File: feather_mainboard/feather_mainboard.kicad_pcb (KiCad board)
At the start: 2 copper layers, 60 x 60 mm, 42 parts, among them J1 62501021721, J2 62501021721, J3 61300211121, J4 693071020811, J5 61300211121, J6 61300211121, J7 61300211121, J8 61300211121, U1 Adafruit ESP32-S3 Feather, U2 SI2307CDS-T1-BE3, U3 2N7002K-T1-GE3, U4 WPME-FISM_SMT-8

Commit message: Corrected/switched the names of MISO and MOSI pins
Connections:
- net /MicroSD-Card Adapter/SD_MISO/CMD renamed /MicroSD-Card Adapter/SD_MOSI/CMD
- net /MicroSD-Card Adapter/SD_MOSI/DAT0 renamed /MicroSD-Card Adapter/SD_MISO/DAT0
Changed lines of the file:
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@@
 	(net 19 "Net-(J6-Pad1)")
 	(net 20 "Net-(J3-Pad1)")
-	(net 21 "/MicroSD-Card Adapter/SD_MISO{slash}CMD")
+	(net 21 "/MicroSD-Card Adapter/SD_MOSI{slash}CMD")
 	(net 22 "/MicroSD-Card Adapter/SD_DAT2")
 	(net 23 "/MicroSD-Card Adapter/SD_CD")
 	(net 24 "/MicroSD-Card Adapter/SD_CLK")
-	(net 25 "/MicroSD-Card Adapter/SD_MOSI{slash}DAT0")
+	(net 25 "/MicroSD-Card Adapter/SD_MISO{slash}DAT0")
 	(net 26 "/MicroSD-Card Adapter/SD_CS{slash}DAT3")
 	(net 27 "/MicroSD-Card Adapter/SD_DAT1")
@@
 			(size 0.7 1.9)
 			(layers "F.Cu" "F.Paste" "F.Mask")
-			(net 21 "/MicroSD-Card Adapter/SD_MISO{slash}CMD")
+			(net 21 "/MicroSD-Card Adapter/SD_MOSI{slash}CMD")
 			(pinfunction "CMD")
 			(pintype "bidirectional")
@@
 			(size 0.7 1.9)
 			(layers "F.Cu" "F.Paste" "F.Mask")
-			(net 25 "/MicroSD-Card Adapter/SD_MOSI{slash}DAT0")
+			(net 25 "/MicroSD-Card Adapter/SD_MISO{slash}DAT0")
 			(pinfunction "DAT0")
 			(pintype "bidirectional")
@@
 			)
 		)
+		(sheetname "Display-Ports")
+		(sheetfile "display_ports.kicad_sch")
 		(attr through_hole)
 		(fp_line
@@
 			(size 0.6 0.9)
 			(layers "F.Cu" "F.Paste" "F.Mask")
-			(net 21 "/MicroSD-Card Adapter/SD_MISO{slash}CMD")
+			(net 21 "/MicroSD-Card Adapter/SD_MOSI{slash}CMD")
 			(pintype "passive")
 			(solder_mask_margin 0.102)
@@
 			)
 		)
+		(sheetname "Buttons-Connector")
+		(sheetfile "buttons-connector.kicad_sch")
 		(attr through_hole)
 		(fp_line
@@
 			(size 0.6 0.9)
 			(layers "F.Cu" "F.Paste" "F.Mask")
-			(net 25 "/MicroSD-Card Adapter/SD_MOSI{slash}DAT0")
+			(net 25 "/MicroSD-Card Adapter/SD_MISO{slash}DAT0")
 			(pintype "passive")
 			(solder_mask_margin 0.102)
@@
 			(layers "*.Cu" "*.Mask")
 			(remove_unused_layers no)
-			(net 21 "/MicroSD-Card Adapter/SD_MISO{slash}CMD")
+			(net 21 "/MicroSD-Card Adapter/SD_MOSI{slash}CMD")
 			(pinfunction "D13")
 			(pintype "bidirectional")
@@
 			(layers "*.Cu" "*.Mask")
 			(remove_unused_layers no)
-			(net 25 "/MicroSD-Card Adapter/SD_MOSI{slash}DAT0")
+			(net 25 "/MicroSD-Card Adapter/SD_MISO{slash}DAT0")
 			(pinfunction "D11")
 			(pintype "bidirectional")

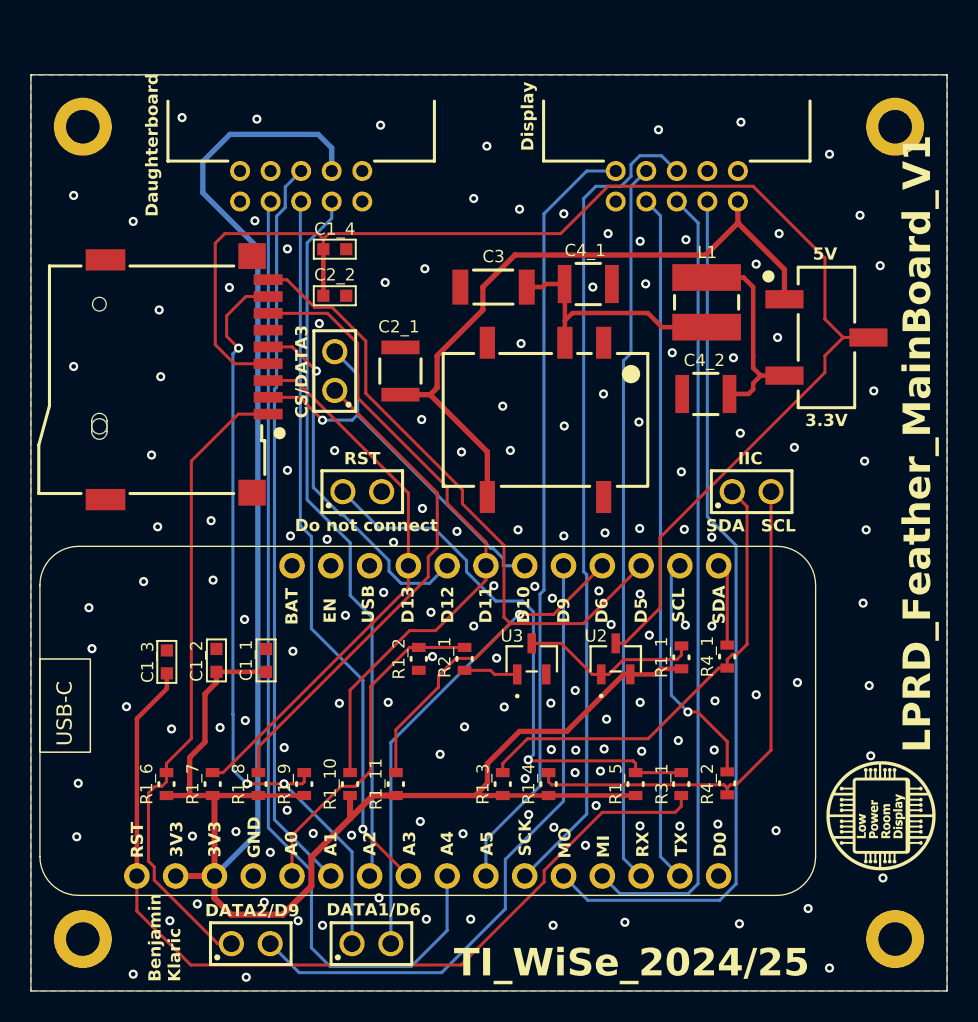
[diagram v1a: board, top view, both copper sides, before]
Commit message: Added V1.1: added a Shottky diode to block the parasitic feedback into the system from the SD adapter; routed the SD adapter pull-ups to the SD Vcc and not the uC Vcc; updated silkscreen text; cleaned routing overall; more vias and more ground plane coverage
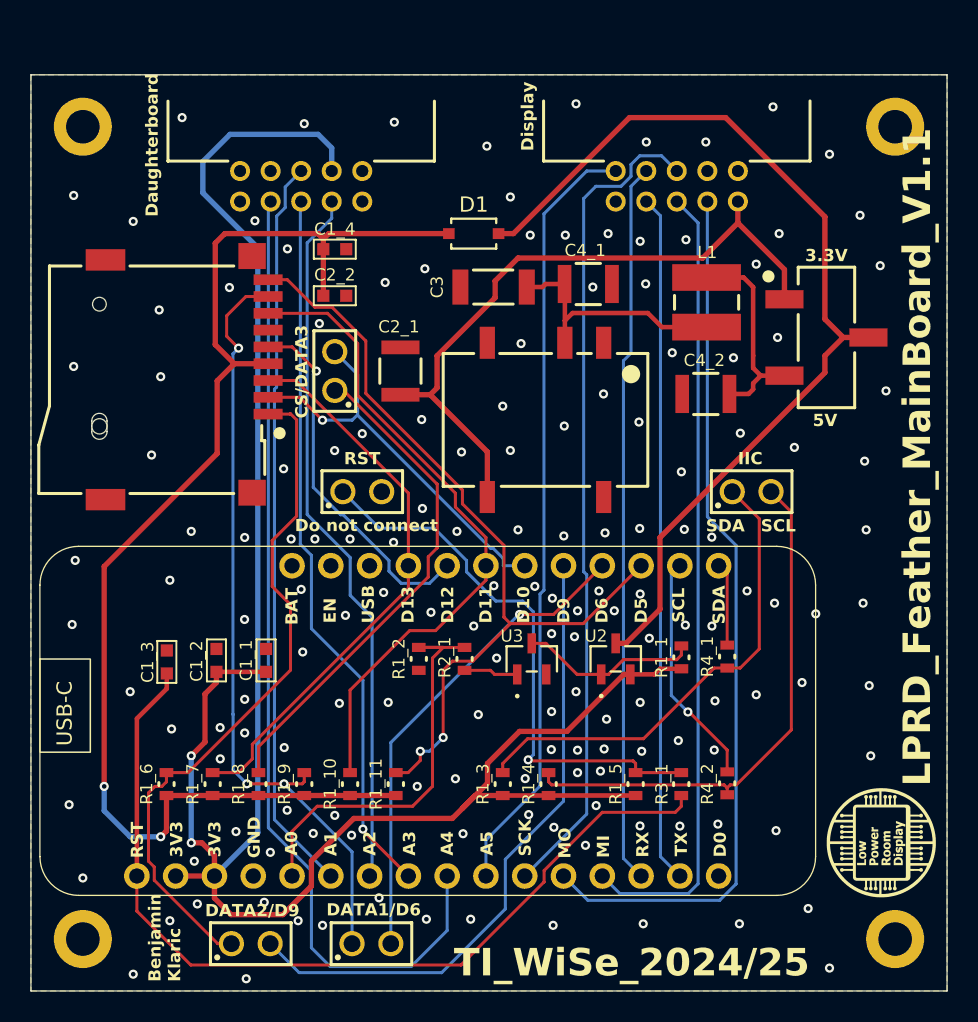
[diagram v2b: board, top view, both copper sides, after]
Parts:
- added D1: PMEG6010CEH_115, Custom footprints:SDO_SOD123F_NEX, F.Cu at (148.8, 79.8)
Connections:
- C1_4 pad 2: /Display-Enable/Switch -> Net-(J4-VDD)
- C2_2 pad 2: /Display-Enable/Switch -> Net-(J4-VDD)
- J4 pad 4: /Display-Enable/Switch -> Net-(J4-VDD)
- R1_10 pad 1: VCC -> Net-(J4-VDD)
- R1_11 pad 1: VCC -> Net-(J4-VDD)
- R1_6 pad 2: VCC -> Net-(J4-VDD)
- R1_7 pad 2: VCC -> Net-(J4-VDD)
- R1_8 pad 2: VCC -> Net-(J4-VDD)
- R1_9 pad 1: VCC -> Net-(J4-VDD)
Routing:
- net Net-(J4-VDD): track 0.00 -> 85.0 mm, vias 0 -> 2
- net /Display-Enable/Switch: track 91.9 -> 63.9 mm
- net VCC: track 142.3 -> 134.0 mm, vias 0 -> 2
- net /Display-Enable/EN: track 22.3 -> 27.3 mm
- net Net-(J4-DAT2): track 42.1 -> 45.2 mm
- net Net-(J6-Pad2): track 33.7 -> 34.8 mm
- net Net-(J6-Pad1): track 30.6 -> 31.5 mm
- net /MicroSD-Card Adapter/SD_CD: track 54.2 -> 55.1 mm, vias 0 -> 2
- net /MicroSD-Card Adapter/SD_MOSI/CMD: track 36.3 -> 36.9 mm
- net GND: vias 147 -> 157
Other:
- board text added: "LPRD_Feather_MainBoard_V1.1"
- board text removed: "LPRD_Feather_MainBoard_V1"

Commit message: Small changes to silkscreen text
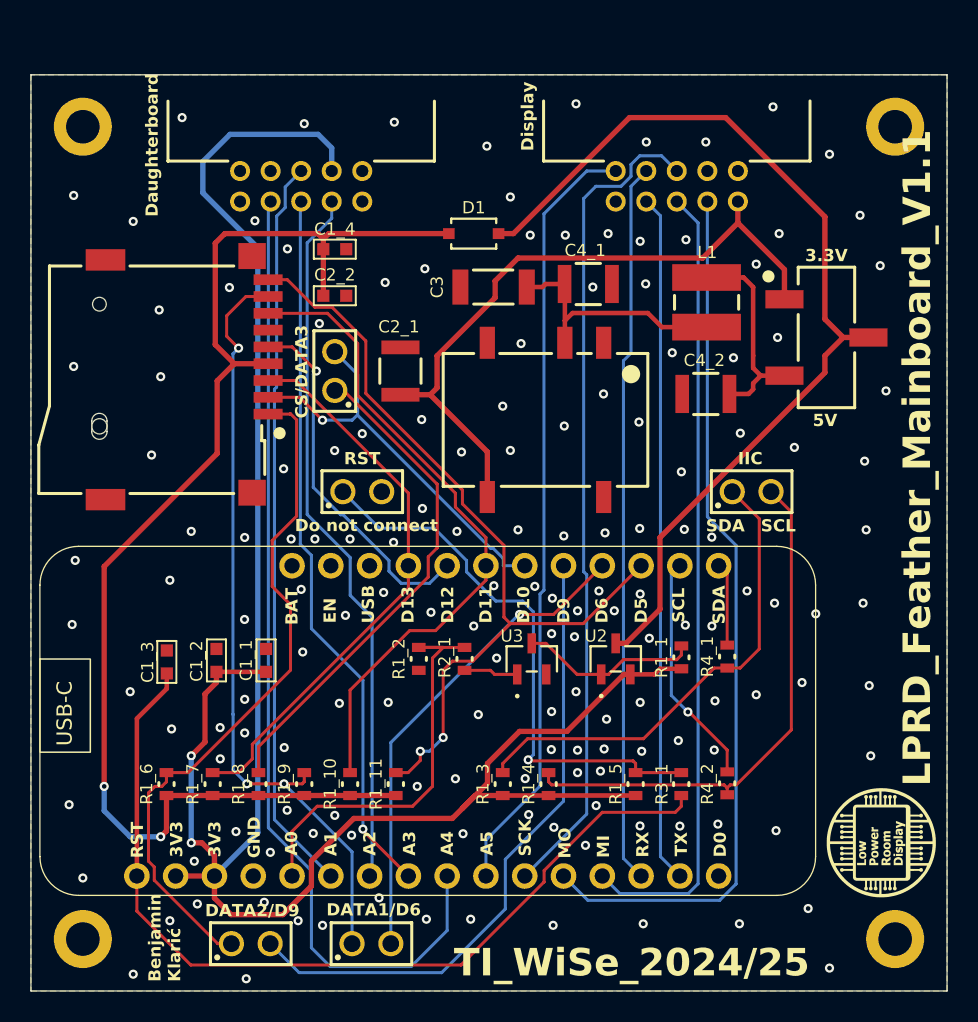
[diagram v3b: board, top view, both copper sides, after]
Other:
- board text added: "Benjamin Klarić"
- board text added: "LPRD_Feather_Mainboard_V1.1"
- board text removed: "Benjamin Klaric"
- board text removed: "LPRD_Feather_MainBoard_V1.1"
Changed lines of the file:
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@@
 		(tags "PMEG6010CEH_115 ")
 		(property "Reference" "D1"
-			(at 0 -1.9 0)
+			(at 0 -1.7 0)
 			(unlocked yes)
 			(layer "F.SilkS")
 			(effects
 				(font
-					(size 1 1)
+					(size 0.8 0.8)
 					(thickness 0.15)
 				)
@@
 			(layer "F.Fab")
 		)
-		(fp_text user "*"
-			(at -1.0922 0 0)
-			(layer "F.Fab")
-			(effects
-				(font
-					(size 1 1)
-					(thickness 0.15)
-				)
-			)
-		)
-		(fp_text user "${REFERENCE}"
-			(at 0 0 0)
-			(unlocked yes)
-			(layer "F.Fab")
-			(effects
-				(font
-					(size 1 1)
-					(thickness 0.15)
-				)
-			)
-		)
-		(fp_text user "*"
-			(at -1.0922 0 0)
-			(unlocked yes)
-			(layer "F.Fab")
-			(effects
-				(font
-					(size 1 1)
-					(thickness 0.15)
-				)
-			)
-		)
 		(pad "1" smd rect
 			(at -1.6256 0)
@@
 		)
 	)
-	(gr_text "LPRD_Feather_MainBoard_V1.1"
+	(gr_text "LPRD_Feather_Mainboard_V1.1"
 		(at 178.9 75.3 90)
 		(layer "B.SilkS")
@@
 		)
 	)
-	(gr_text "LPRD_Feather_MainBoard_V1.1"
+	(gr_text "LPRD_Feather_Mainboard_V1.1"
 		(at 178.9 116 90)
 		(layer "F.SilkS")
@@
 		)
 	)
-	(gr_text "Benjamin\nKlaric"
+	(gr_text "Benjamin\nKlarić"
 		(at 129.675 128.8 90)
 		(layer "F.SilkS")

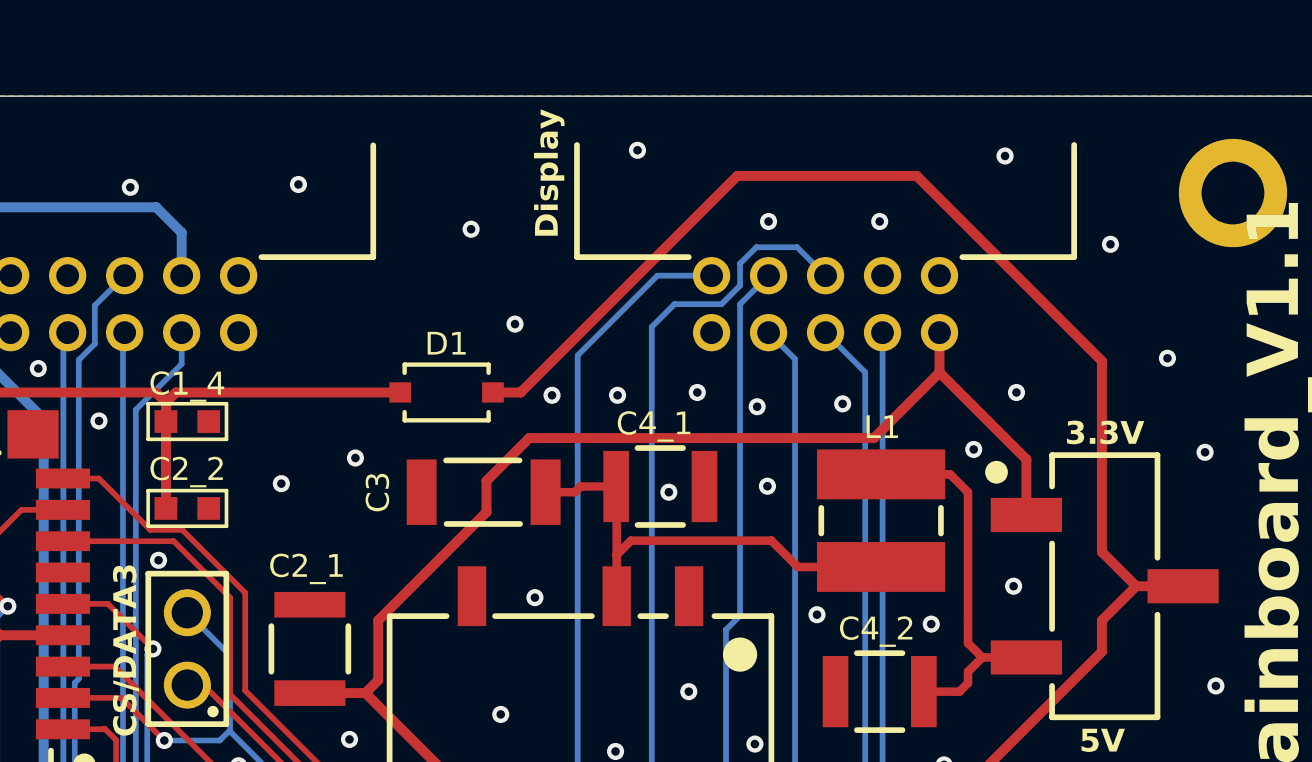
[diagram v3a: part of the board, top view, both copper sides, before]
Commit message: Removed the diode, since it is not needed
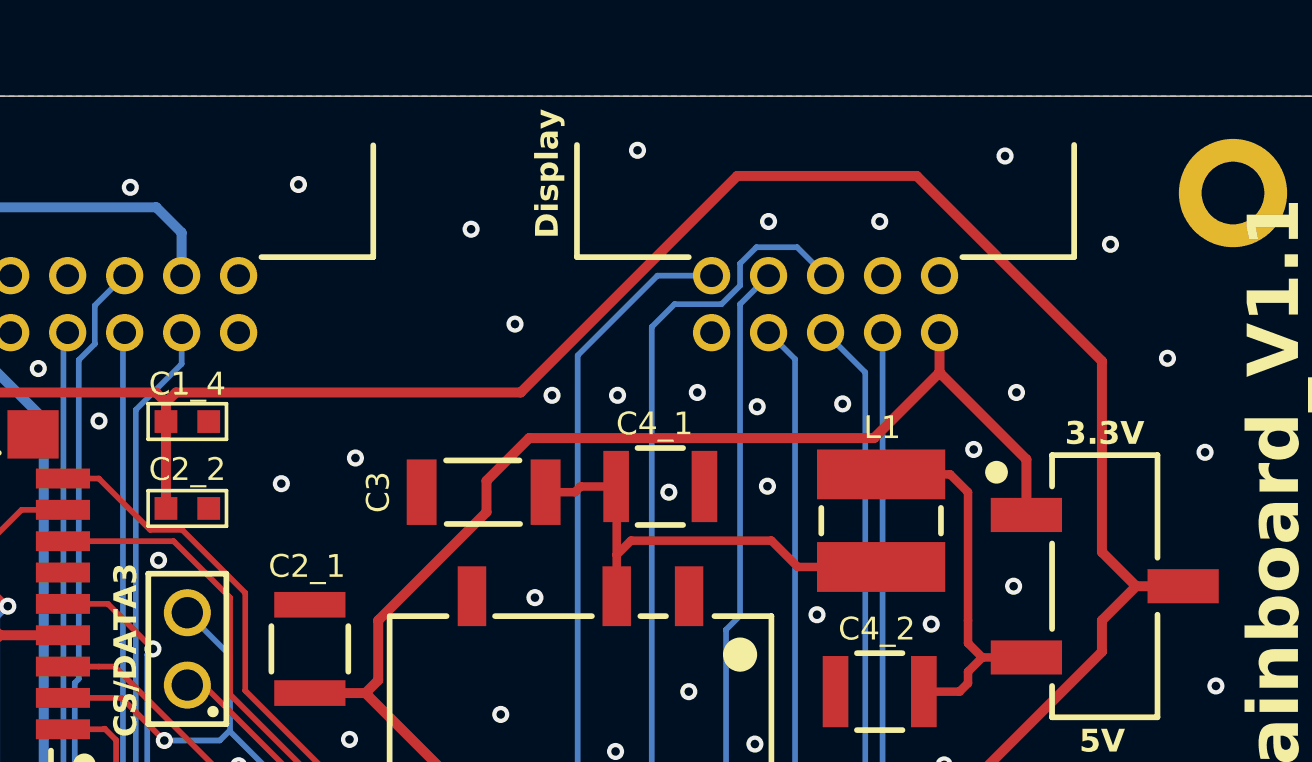
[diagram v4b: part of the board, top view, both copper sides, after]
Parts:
- removed D1: PMEG6010CEH_115, Custom footprints:SDO_SOD123F_NEX
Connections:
- C1_4 pad 2: Net-(J4-VDD) -> /Display-Enable/Switch
- C2_2 pad 2: Net-(J4-VDD) -> /Display-Enable/Switch
- J4 pad 4: Net-(J4-VDD) -> /Display-Enable/Switch
- R1_10 pad 1: Net-(J4-VDD) -> /Display-Enable/Switch
- R1_11 pad 1: Net-(J4-VDD) -> /Display-Enable/Switch
- R1_6 pad 2: Net-(J4-VDD) -> /Display-Enable/Switch
- R1_7 pad 2: Net-(J4-VDD) -> /Display-Enable/Switch
- R1_8 pad 2: Net-(J4-VDD) -> /Display-Enable/Switch
- R1_9 pad 1: Net-(J4-VDD) -> /Display-Enable/Switch
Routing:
- net /Display-Enable/Switch: track 63.9 -> 152.1 mm, vias 0 -> 2
- net Net-(J4-VDD): track 85.0 -> 0.00 mm, vias 2 -> 0
